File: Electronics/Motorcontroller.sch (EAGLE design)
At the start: 45 parts, among them Q1 IRFZ48V, Q2 IRF4905V, Q3 IRFZ48V, Q4 IRF4905V, Q5 IRFZ48V, Q6 IRF4905V, Q7 IRFZ48V, Q8 IRF4905V, T1 BC547, T2 BC547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

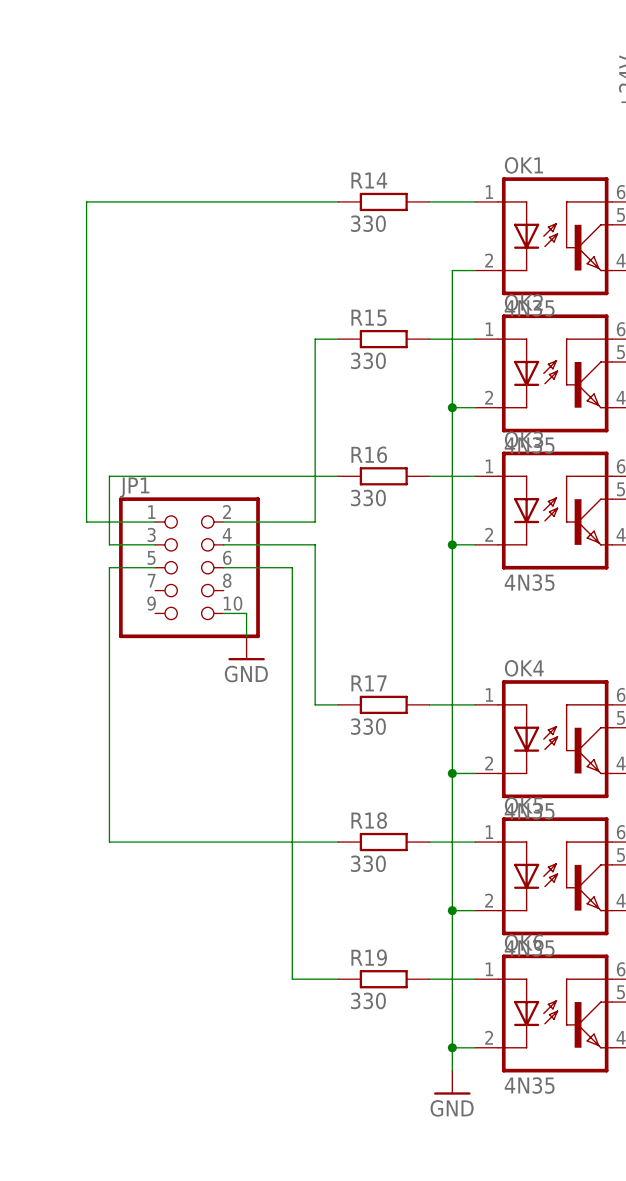
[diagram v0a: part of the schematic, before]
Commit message: Added LEDs to optocoupelers. Closes #39
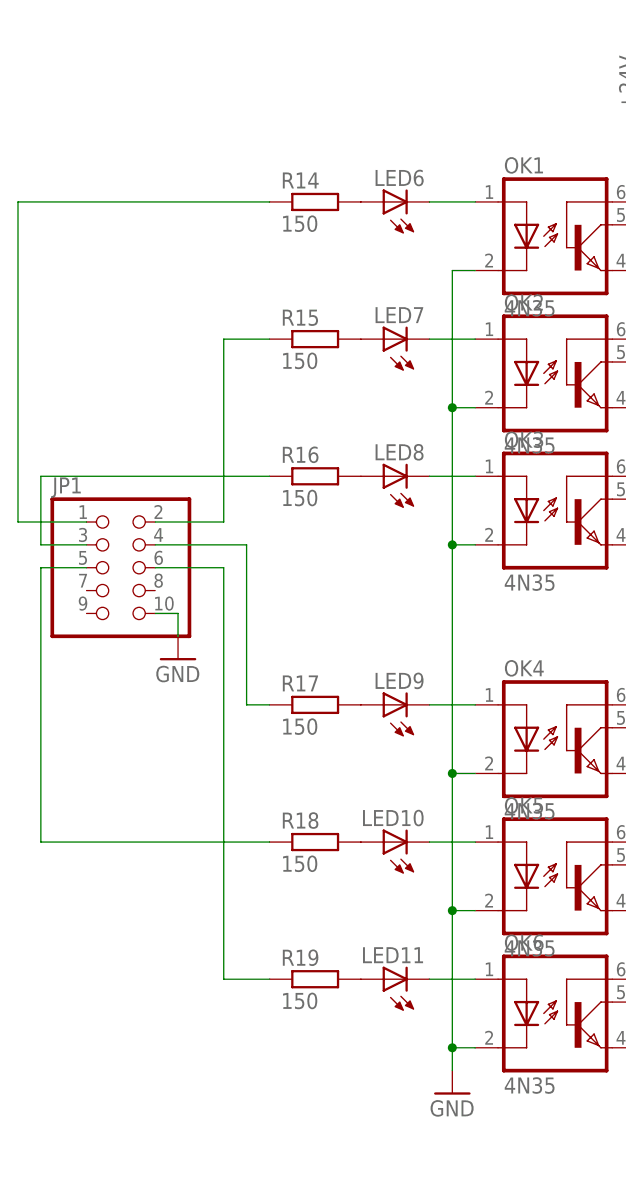
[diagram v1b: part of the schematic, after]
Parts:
- added LED10, LED11, LED6, LED7, LED8, LED9: (no value), led:LED3MM
- R14, R19: value 330 -> 150
- R15, R16, R17, R18: value 330 -> 150; device rcl:R-EU_0207/7 -> rcl:R-EU_0207/5V
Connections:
- removed net N$36: OK5.A, R18.2
- removed net N$37: OK6.A, R19.2
- new net N$17: LED10.A, R18.2
- new net N$20: LED6.A, R14.2
- new net N$26: LED7.A, R15.2
- new net N$27: LED8.A, R16.2
- new net N$28: LED9.A, R17.2
- new net N$33: LED9.C, OK4.A
- new net N$34: LED10.C, OK5.A
- new net N$35: LED11.C, OK6.A
- net N$29: now also LED11.A, R19.2; no longer OK1.A, R14.2
- net N$30: now also LED6.C, OK1.A; no longer OK2.A, R15.2
- net N$31: now also LED7.C, OK2.A; no longer OK3.A, R16.2
- net N$32: now also LED8.C, OK3.A; no longer OK4.A, R17.2
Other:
- moved on the sheet: JP1, R14, R15, R16, R17, R18, R19

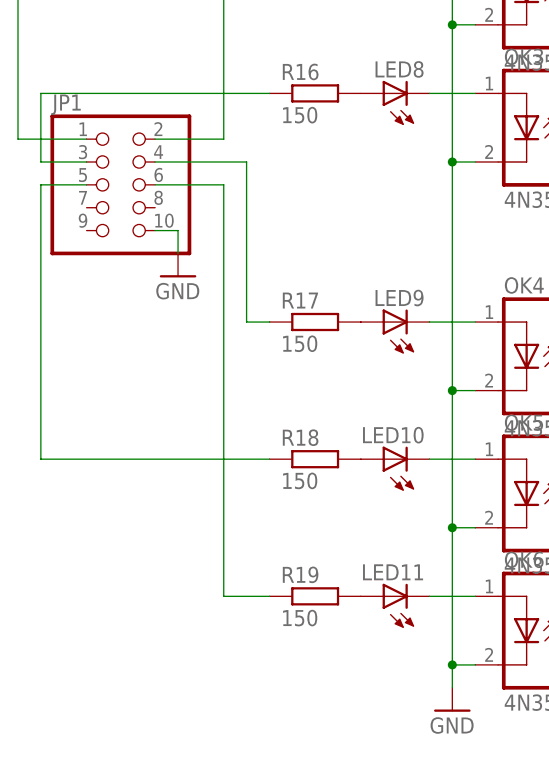
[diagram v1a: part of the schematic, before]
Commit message: Changed pins on pinheader
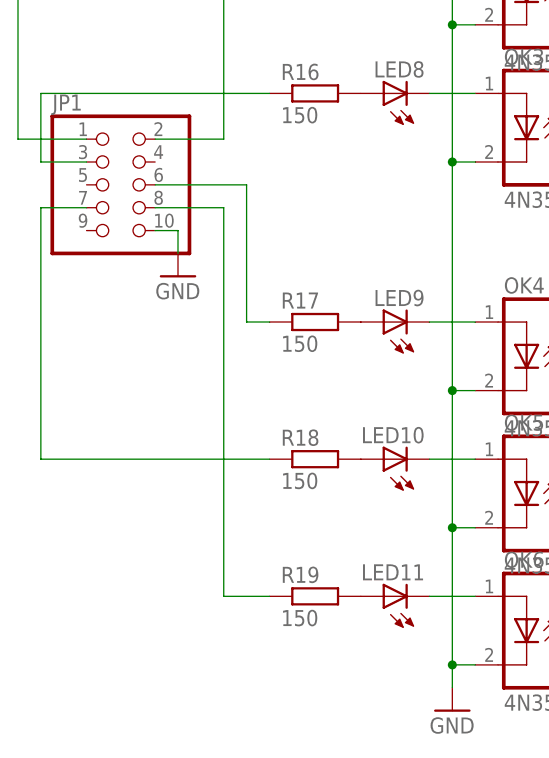
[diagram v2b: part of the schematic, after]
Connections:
- net N$10: now also JP1.7; no longer JP1.5
- net N$11: now also JP1.8; no longer JP1.6
- net N$8: now also JP1.6; no longer JP1.4
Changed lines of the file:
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@@
 <net name="N$8" class="0">
 <segment>
-<pinref part="JP1" gate="A" pin="4"/>
 <pinref part="R17" gate="G$1" pin="1"/>
-<wire x1="129.54" y1="91.44" x2="119.38" y2="91.44" width="0.1524" layer="91"/>
 <wire x1="132.08" y1="73.66" x2="129.54" y2="73.66" width="0.1524" layer="91"/>
-<wire x1="129.54" y1="73.66" x2="129.54" y2="91.44" width="0.1524" layer="91"/>
+<wire x1="129.54" y1="73.66" x2="129.54" y2="88.9" width="0.1524" layer="91"/>
+<pinref part="JP1" gate="A" pin="6"/>
+<wire x1="119.38" y1="88.9" x2="129.54" y2="88.9" width="0.1524" layer="91"/>
 </segment>
 </net>
 <net name="N$10" class="0">
 <segment>
-<wire x1="106.68" y1="58.42" x2="106.68" y2="88.9" width="0.1524" layer="91"/>
-<pinref part="JP1" gate="A" pin="5"/>
-<wire x1="106.68" y1="88.9" x2="111.76" y2="88.9" width="0.1524" layer="91"/>
+<wire x1="106.68" y1="58.42" x2="106.68" y2="86.36" width="0.1524" layer="91"/>
 <pinref part="R18" gate="G$1" pin="1"/>
 <wire x1="106.68" y1="58.42" x2="132.08" y2="58.42" width="0.1524" layer="91"/>
+<pinref part="JP1" gate="A" pin="7"/>
+<wire x1="111.76" y1="86.36" x2="106.68" y2="86.36" width="0.1524" layer="91"/>
 </segment>
 </net>
 <net name="N$11" class="0">
 <segment>
-<wire x1="127" y1="43.18" x2="127" y2="88.9" width="0.1524" layer="91"/>
-<pinref part="JP1" gate="A" pin="6"/>
-<wire x1="127" y1="88.9" x2="119.38" y2="88.9" width="0.1524" layer="91"/>
 <pinref part="R19" gate="G$1" pin="1"/>
 <wire x1="132.08" y1="43.18" x2="127" y2="43.18" width="0.1524" layer="91"/>
+<pinref part="JP1" gate="A" pin="8"/>
+<wire x1="119.38" y1="86.36" x2="127" y2="86.36" width="0.1524" layer="91"/>
+<wire x1="127" y1="86.36" x2="127" y2="43.18" width="0.1524" layer="91"/>
 </segment>
 </net>

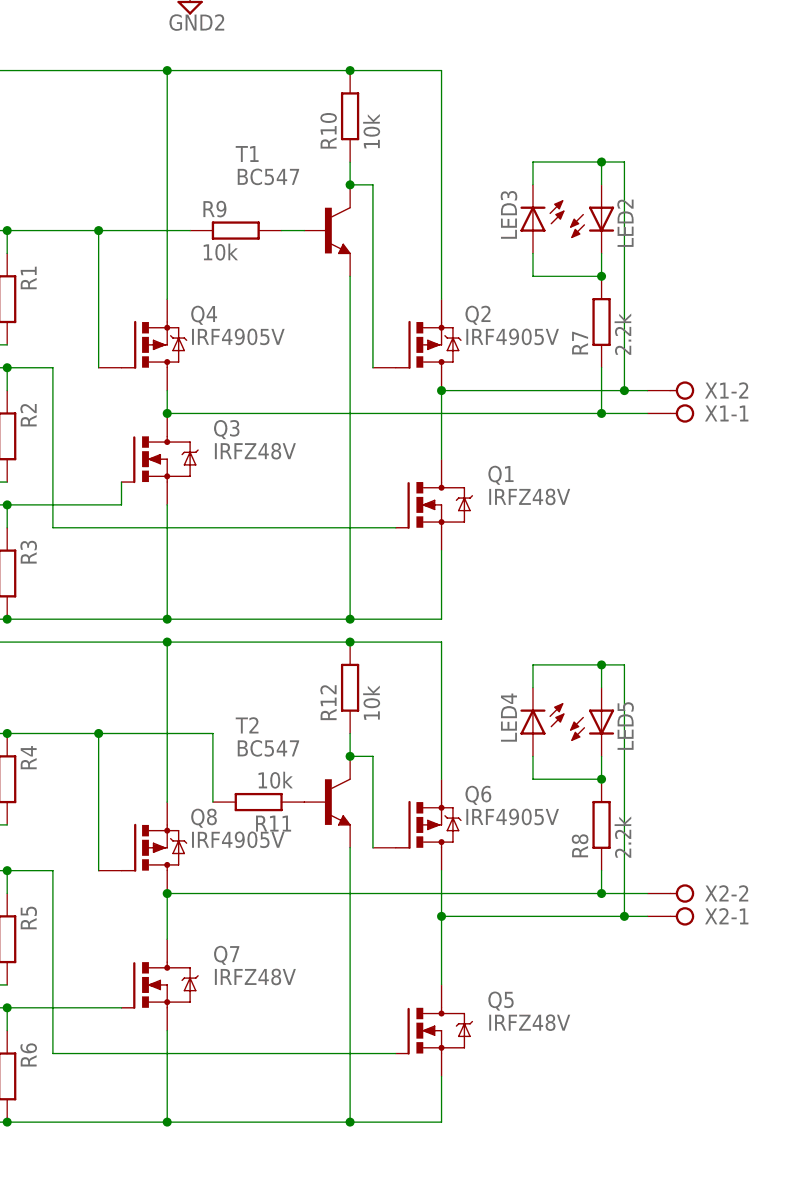
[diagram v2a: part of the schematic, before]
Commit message: Motorcontroller with protection diodes. Also closes #40
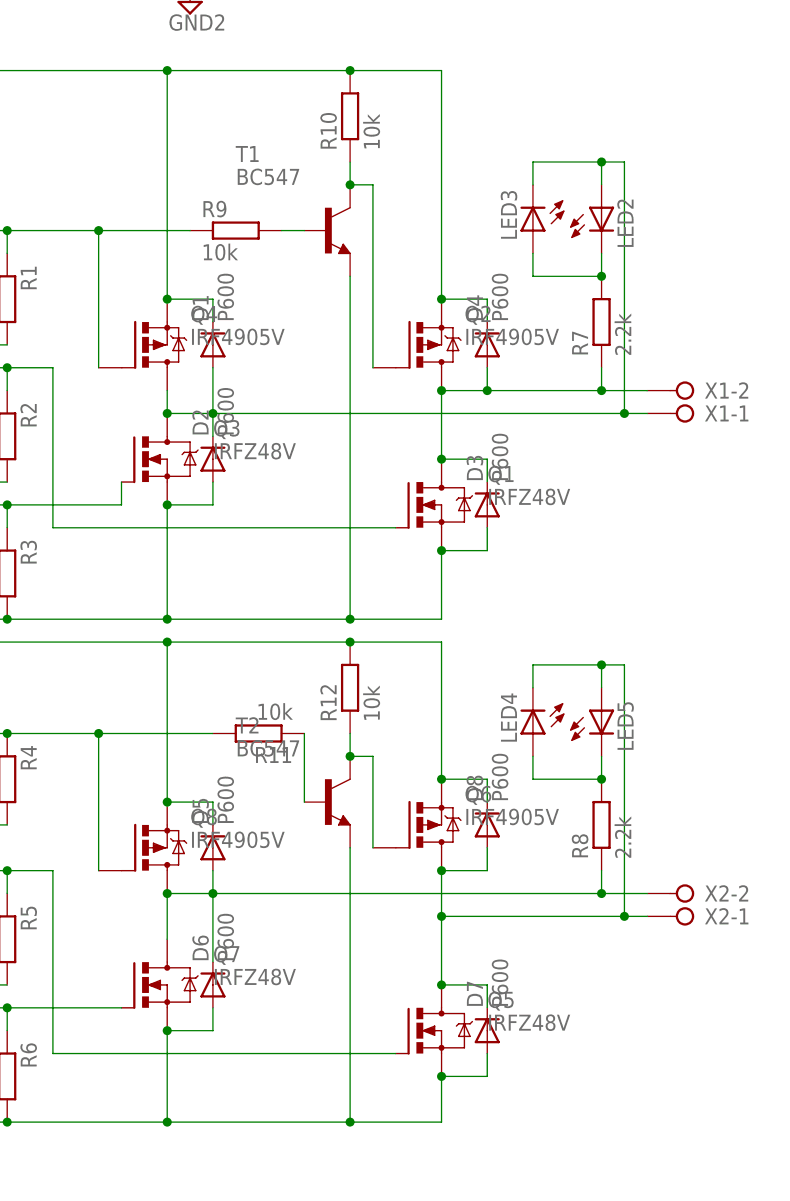
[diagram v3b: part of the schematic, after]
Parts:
- added D1, D2, D3, D4, D5, D6, D7, D8: P600, diode:P600
- R13: device rcl:R-EU_0207/10 -> rcl:R-EU_0207/2V
- R7, R8: device rcl:R-EU_0207/7 -> rcl:R-EU_0207/2V
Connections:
- removed net N$2: Q3.D, Q4.D, R7.1, X1-1.KL
- removed net N$25: Q7.D, Q8.D, R8.1, X2-2.KL
- new net N$36: D1.A, D2.C, LED2.A, LED3.C, Q3.D, Q4.D, X1-1.KL
- new net N$43: D5.A, D6.C, Q7.D, Q8.D, R8.1, X2-2.KL
- net +24V: now also D1.C, D4.C, D5.C, D8.C
- net GND2: now also D2.A, D3.A, D6.A, D7.A
- net N$1: now also D7.C, D8.A
- net N$4: now also D3.C, D4.A, R7.1; no longer LED2.A, LED3.C
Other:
- moved on the sheet: R11

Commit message: Reset to motorcontroller v5.2
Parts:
- removed D1, D2, D3, D4, D5, D6, D7, D8: P600, diode:P600
- R13: device rcl:R-EU_0207/2V -> rcl:R-EU_0207/10
- R7, R8: device rcl:R-EU_0207/2V -> rcl:R-EU_0207/7
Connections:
- removed net N$36: D1.A, D2.C, LED2.A, LED3.C, Q3.D, Q4.D, X1-1.KL
- removed net N$43: D5.A, D6.C, Q7.D, Q8.D, R8.1, X2-2.KL
- new net N$2: Q3.D, Q4.D, R7.1, X1-1.KL
- new net N$25: Q7.D, Q8.D, R8.1, X2-2.KL
- net +24V: no longer D1.C, D4.C, D5.C, D8.C
- net GND2: no longer D2.A, D3.A, D6.A, D7.A
- net N$1: no longer D7.C, D8.A
- net N$4: now also LED2.A, LED3.C; no longer D3.C, D4.A, R7.1
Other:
- moved on the sheet: R11
